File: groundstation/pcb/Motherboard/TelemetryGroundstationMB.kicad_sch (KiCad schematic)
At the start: 109 parts, among them J1 USB-C, J2 USB-C, J3 ICD15S13E4GV00LF, M1 M4 Mounting Hole, M2 M4 Mounting Hole, M3 M4 Mounting Hole, M4 M4 Mounting Hole, Q1 NPN, U1 CP2102N, U2 CP2102N, U5 AVR128DB64x-xPT

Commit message: update motherboard
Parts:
- removed D19, D20, D21, D22, D23, D24: red, LED_SMD:LED_0805_2012Metric_Pad1.15x1.40mm_HandSolder, symbol Device:LED
- removed D25, D26: orange, LED_SMD:LED_0805_2012Metric_Pad1.15x1.40mm_HandSolder, symbol Device:LED
- removed R32, R33, R35, R36, R43, R44: 1k, Resistor_SMD:R_0805_2012Metric_Pad1.20x1.40mm_HandSolder, symbol Device:R
- removed R34, R37, R38, R39, R40, R41, R42, R49, R50: 5k6, Resistor_SMD:R_0805_2012Metric_Pad1.20x1.40mm_HandSolder, symbol Device:R
- removed R45, R46: 270R, Resistor_SMD:R_0805_2012Metric_Pad1.20x1.40mm_HandSolder, symbol Device:R
- removed TP12, TP13, TP14, TP15, TP16, TP17, TP36, TP37, TP38, TP39, TP4, TP5, TP60, TP70, TP8, TP80, TP9: TestPoint, Footprints:Test Point, symbol Connector:TestPoint
- added C13, C14: 100uF Elko, Capacitor_THT:CP_Radial_D6.3mm_P2.50mm, symbol Device:C_Polarized
- added C5: 0.1 uF, Capacitor_SMD:C_0805_2012Metric_Pad1.18x1.45mm_HandSolder, symbol Device:C
- added C6: 4.7 uF, Capacitor_SMD:C_0805_2012Metric_Pad1.18x1.45mm_HandSolder, symbol Device:C
- added C7, C8: 10uF Tantal, Bibliothek:CAPMP3216X180N, symbol Device:C_Polarized
- added D14: SP0503BAHT, Package_TO_SOT_SMD:SOT-143, symbol Power_Protection:SP0503BAHT
- added D15: green, LED_SMD:LED_0805_2012Metric_Pad1.15x1.40mm_HandSolder, symbol Device:LED
- added D16, D29, D30, D31, D32, D33, D34: orange, LED_SMD:LED_0805_2012Metric_Pad1.15x1.40mm_HandSolder, symbol Device:LED
- added J4: USB-C, Footprints:GCT_USB4216-03-A_REVA, symbol Symbols:USB4216-03-A_REVA
- added J5, J6, J7: ICD15S13E4GV00LF, Footprints:AMPHENOL_ICD15S13E4GV00LF[1], symbol Symbols:ICD15S13E4GV00LF
- added J8: Conn_01x06_Pin, symbol Connector:Conn_01x06_Pin
- added JP3: SolderJumper_2_Open, Footprints:Solder Jumper, symbol Jumper:SolderJumper_2_Open
- added R22, R27: 5k1, Resistor_SMD:R_0805_2012Metric_Pad1.20x1.40mm_HandSolder, symbol Device:R
- added R23: 22k, Resistor_SMD:R_0805_2012Metric_Pad1.20x1.40mm_HandSolder, symbol Device:R
- added R24: 47k, Resistor_SMD:R_0805_2012Metric_Pad1.20x1.40mm_HandSolder, symbol Device:R
- added R25, R26: 560 Ohm, Resistor_SMD:R_0805_2012Metric_Pad1.20x1.40mm_HandSolder, symbol Device:R
- added R51, R52, R53, R54, R55, R56: 270R, Resistor_SMD:R_0805_2012Metric_Pad1.20x1.40mm_HandSolder, symbol Device:R
- added TP6, TP7: TestPoint, Footprints:Test Point, symbol Connector:TestPoint
- added U3: CP2102N, Footprints:QFN20_CP2102N_SIL, symbol Interface_USB:CP2102N-Axx-xQFN20
- added U4: MIC29300-5WU-TR, Footprints:MIC29300, symbol Symbols:MIC29300-3.3WU-TR
- added U6: MIC29300-3.3WU-TR, Footprints:MIC29300, symbol Symbols:MIC29300-3.3WU-TR
- D11, D12, R20, R21: now fitted
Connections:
- net D1 is gone; now on net D01: J3.1
- net D27 is gone; now on net D21: U5.49 (PF5)
- net MISO0 is gone; now on net RX4: U5.37 (PE1)
- net MOSI0 is gone; now on net TX4: U5.36 (PE0)
- net RST1 is gone; now on net D02: U5.1 (PA3)
- net RST2 is gone; now on net D31: U5.12 (PB4)
- net RTS2 is gone; now on net D31: U5.13 (PB5)
- net RX is gone; now on net RX0: J3.7
- net TX is gone; now on net TX0: J3.6
- net +3V3: now also C5.1, C6.1, C7.1, C8.1, D15.2 (A), D16.2 (A), J5.11, J5.5, J5.8, J6.11, J6.5, J6.8, J7.11, J7.5, J7.8, U3.6 (VDD), U3.7 (VREGIN), U4.3 (OUT), U6.3 (OUT)
- net +5V: now also J5.10, J5.13, J5.15, J6.10, J6.13, J6.15, J7.10, J7.13, J7.15
- net BUZZ: no longer U5.9 (PB1)
- net GND: now also C13.2, C14.2, C5.2, C6.2, C7.2, C8.2, D14.1 (A), D29.1 (K), D30.1 (K), D31.1 (K), D33.1 (K), D34.1 (K), J4.A1_B12 (GND_A), J4.B1_A12 (GND_B), J4.SH1 (SHIELD), J4.SH2 (SHIELD), J4.SH3 (SHIELD), J4.SH4 (SHIELD), J5.12, J5.14, J5.9, J5.SH1 (SHIELD), J5.SH2 (SHIELD__1), J6.12, J6.14, J6.9, J6.SH1 (SHIELD), J6.SH2 (SHIELD__1), J7.12, J7.14, J7.9, J7.SH1 (SHIELD), J7.SH2 (SHIELD__1), JP3.2 (B), R22.2, R24.2, R27.2, U3.12 (GND), U3.21 (GND), U3.3 (GND), U4.1 (IN), U4.4, U6.1 (IN), U6.4
- net LED 1: no longer U5.45 (XTAL32K2/PF1)
- net LED 2: no longer U5.46 (PF2)
- net LED 3: no longer U5.47 (PF3)
- net LED B: no longer U5.42 (PE6)
- net LED G: no longer U5.43 (PE7)
- net LED R: no longer U5.44 (XTAL32K1/PF0)
- net RX0: now also U5.63 (XTALHF2/PA1); no longer U5.3 (PA5)
- net RX1: now also J5.7
- net RX4: no longer U5.41 (PE5)
- net TX0: now also U5.62 (XTALHF1/PA0); no longer U5.2 (PA4)
- net TX1: now also J5.6
- net TX4: no longer U5.40 (PE4)
- net D31: now reaches U5.10 (PB2)
- net D31: now also U5.11 (PB3), J7.1
- net SDA0: now reaches U5.24 (PC6)
- net SDA0: now also R31.1
- net SCL0: now reaches U5.25 (PC7)
- net SCL0: now also R30.1
- net at U5.27 (PD1): now also R48.2
- net at U5.28 (PD2): now also R51.2
- net at U5.29 (PD3): now also R52.2
- net at U5.30 (PD4): now also R53.2
- net at U5.31 (PD5): now also R54.2
- net at U5.32 (PD6): now also R55.2; no longer R48.2
- net at U5.33 (VREFA/PD7): now also R56.2
- net at U5.54 (PG2): now also J8.1 (Pin_1)
- net at U5.55 (PG3): now also J8.2 (Pin_2)
- net at U5.58 (PG4): now also J8.3 (Pin_3)
- net at U5.59 (PG5): now also J8.4 (Pin_4)
- net at U5.60 (PG6): now also J8.5 (Pin_5)
- net at U5.61 (PG7): now also J8.6 (Pin_6)
- net D01: now reaches U5.64 (PA2)
- net ARM1 renamed RX5
- net RX5: now also TP7.1, U3.18 (TXD)
- net CFG1: no longer names the net of U5.5 (PA7)
- net CFG2: no longer names the net of U5.15 (PB7)
- net CS0 renamed LED2
- net CTS1: no longer names the net of U5.4 (PA6)
- net CTS2: no longer names the net of U5.14 (PB6)
- net D2 renamed D02
- net D26 renamed D21
- net D21: now also U5.46 (PF2), U5.47 (PF3), J6.1
- net D28: no longer names the net of U5.50 (~{RESET}/PF6)
- net D3 renamed D03
- net D03: now also U5.2 (PA4)
- net D4 renamed D04
- net D04: now also U5.3 (PA5); no longer U5.22 (PC4)
- net D5 renamed D14
- net D14: now also J5.4
- net RTS1 renamed TX3
- net TX3: now also J7.6
- net SCK0 renamed LED1
- net SCL1 renamed D12
- net D12: now also J5.2; no longer R30.1
- net SDA1 renamed D11
- net D11: now also J5.1; no longer R31.1
- net SLP renamed TX5
- net TX5: now also TP6.1, U3.17 (RXD)
- new net: D29.2 (A), R51.1
- new net: D30.2 (A), R52.1
- new net: R23.2, R24.1, U3.8 (VBUS)
- new net: D34.2 (A), R56.1
- new net: D32.2 (A), R54.1
- new net: J4.A5 (CC1), R22.1
- new net: J4.B5 (CC2), R27.1
- new net: D16.1 (K), R26.1
- new net: R26.2, U3.19 (~{RXT}/GPIO.3)
- new net: D33.2 (A), R55.1
- new net: D15.1 (K), R25.1
- new net: D31.2 (A), R53.1
- new net: JP3.1 (A), U3.15 (~{CTS})
- new net: R25.2, U3.20 (~{TXT}/GPIO.2)
- new net +BATT: C13.1, C14.1, U4.2 (GND), U6.2 (GND)
- new net D+3: D14.4 (K), J4.A6 (DP1), J4.B6 (DP2), U3.4 (D+)
- new net D-3: D14.3 (K), J4.A7 (DN1), J4.B7 (DN2), U3.5 (D-)
- new net D13: J5.3, U5.22 (PC4)
- new net D22: J6.2
- new net D23: J6.3
- new net D24: J6.4
- new net D32: J7.2
- new net D33: J7.3
- new net D34: J7.4
- new net LED3: U5.40 (PE4)
- new net LEDB: U5.41 (PE5)
- new net LEDG: U5.42 (PE6)
- new net LEDR: U5.43 (PE7)
- new net RX2: J6.7, U5.45 (XTAL32K2/PF1)
- new net RX3: J7.7, U5.9 (PB1)
- new net TX2: J6.6, U5.44 (XTAL32K1/PF0)
- new net VBUS3: D14.2 (K), J4.A4_B9 (VBUS_A), J4.B4_A9 (VBUS_B), R23.1
- no-connect marks 36 -> 28
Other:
- note added: "ESD Protection"
- note added: "HD15 D-SUB Connector"
- note added: "Power supply"
- note removed: "Pinheader?"
- note removed: "Test Points"
- moved on the sheet: J3, R30, R31

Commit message: update motherboard
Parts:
- removed D18: D, Diode_SMD:D_SOD-123, symbol Device:D
- removed LS1: Buzzer CMT-0525-75-SMT-TR, Footprints:Buzzer XDCR_CMT-0525-75-SMT-TR, symbol Symbols:Buzzer CMT-0525-75-SMT-TR
- removed Q1: NPN, Package_TO_SOT_SMD:SOT-23, symbol Simulation_SPICE:NPN
- removed R29: 180 R, Resistor_SMD:R_0805_2012Metric_Pad1.20x1.40mm_HandSolder, symbol Device:R
- added J9: Conn_01x04_Socket, symbol Connector:Conn_01x04_Socket
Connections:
- net +5V: now also J9.3 (Pin_3)
- net GND: now also J9.4 (Pin_4)
- net SCL0: now also J9.1 (Pin_1)
- net SDA0: now also J9.2 (Pin_2)
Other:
- note removed: "Buzzer"

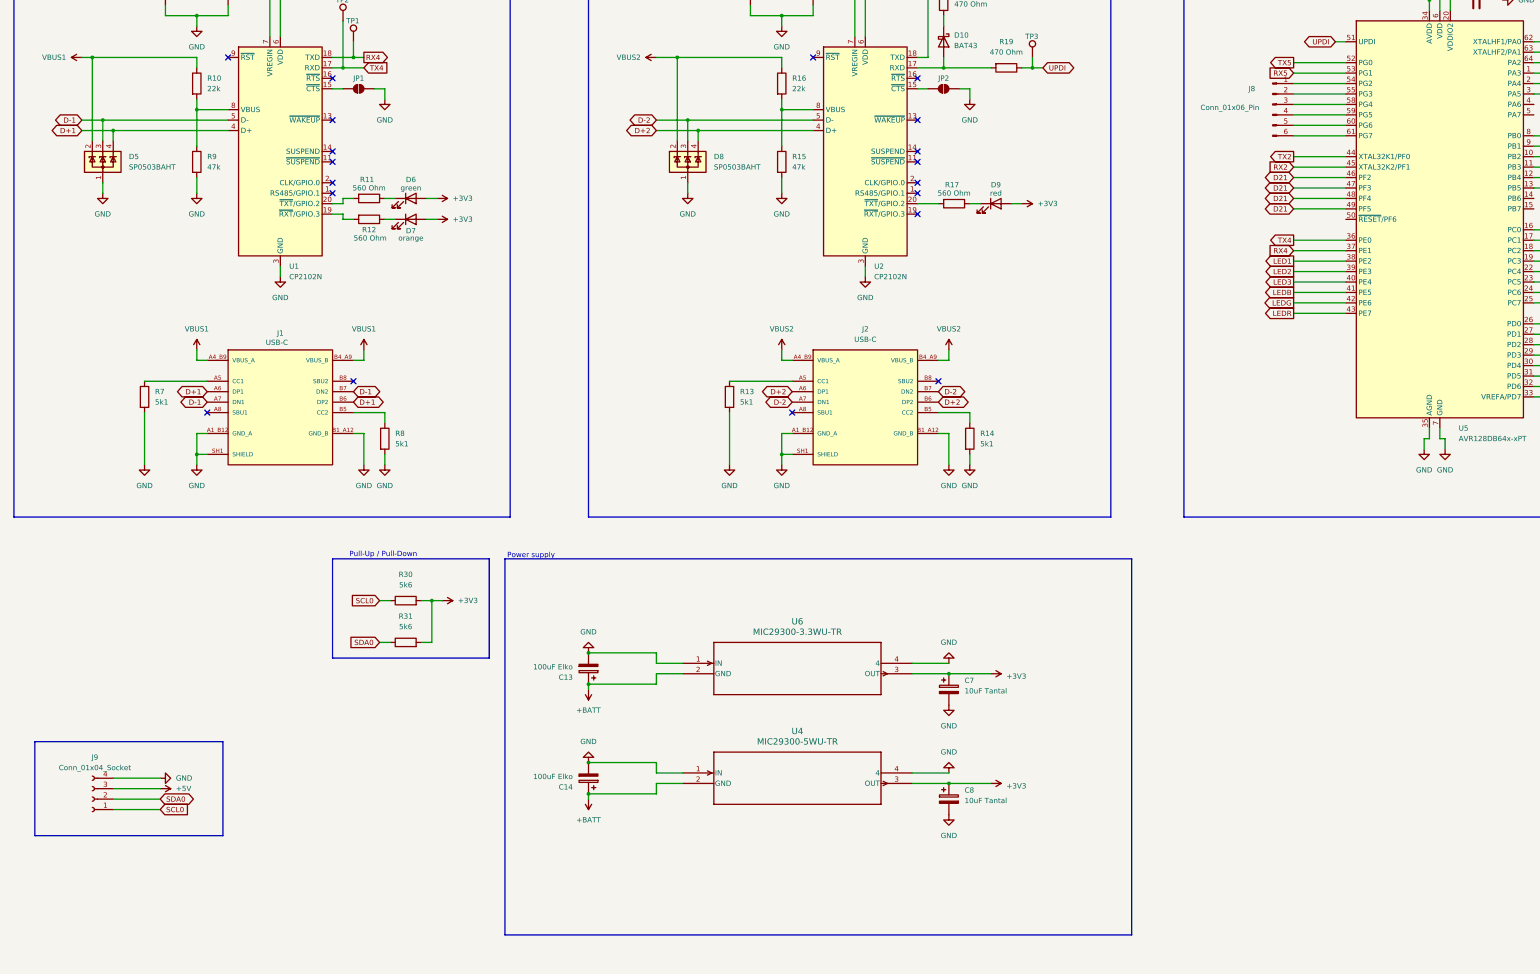
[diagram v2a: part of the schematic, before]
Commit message: add 6 buttons to motherboard
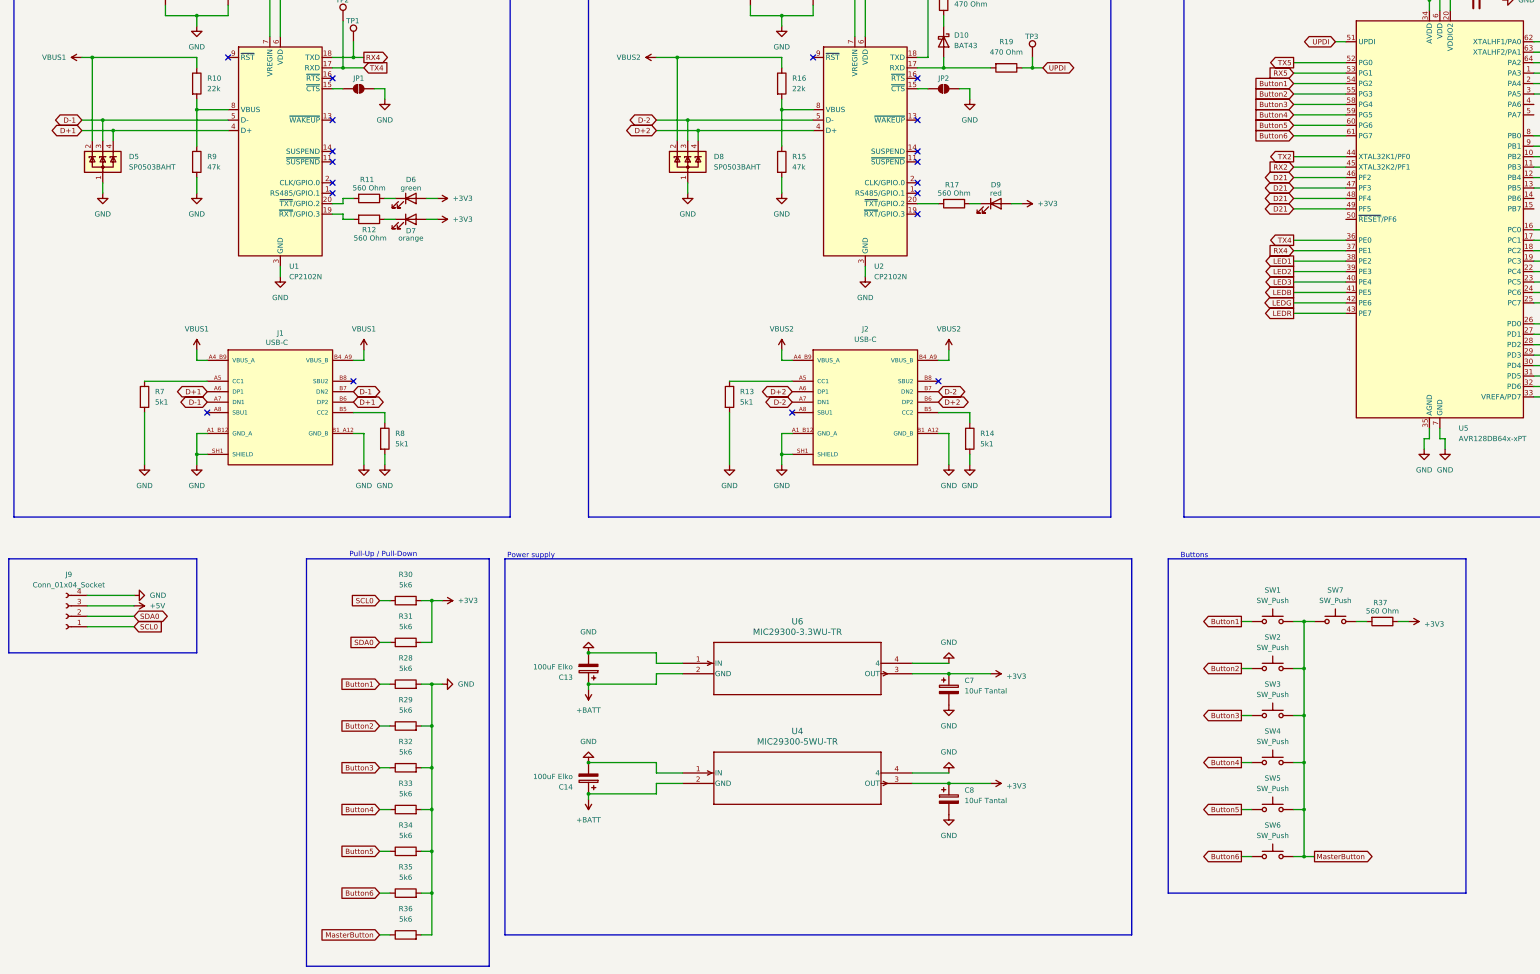
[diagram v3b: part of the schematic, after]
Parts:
- removed J8: Conn_01x06_Pin, symbol Connector:Conn_01x06_Pin
- added R28, R29, R32, R33, R34, R35, R36: 5k6, Resistor_SMD:R_0805_2012Metric_Pad1.20x1.40mm_HandSolder, symbol Device:R
- added R37: 560 Ohm, Resistor_SMD:R_0805_2012Metric_Pad1.20x1.40mm_HandSolder, symbol Device:R
- added SW1, SW2, SW3, SW4, SW5, SW6, SW7: SW_Push, symbol Switch:SW_Push
- R47, R48, R51, R52, R53, R54, R55, R56: value 270R -> 560 Ohm
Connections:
- net +3V3: now also R37.1
- net GND: now also R28.2, R29.2, R32.2, R33.2, R34.2, R35.2, R36.2
- net Button1: now reaches U5.54 (PG2)
- net Button1: now also R28.1, SW1.1
- net Button2: now reaches U5.55 (PG3)
- net Button2: now also R29.1, SW2.1
- net Button3: now reaches U5.58 (PG4)
- net Button3: now also R32.1, SW3.1
- net Button4: now reaches U5.59 (PG5)
- net Button4: now also R33.1, SW4.1
- net Button5: now reaches U5.60 (PG6)
- net Button5: now also R34.1, SW5.1
- net Button6: now reaches U5.61 (PG7)
- net Button6: now also R35.1, SW6.1
- new net: R37.2, SW7.2
- new net MasterButton: R36.1, SW1.2, SW2.2, SW3.2, SW4.2, SW5.2, SW6.2, SW7.1
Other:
- note added: "Buttons"
- moved on the sheet: J9

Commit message: include input from ignition system
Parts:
- added J8: Conn_01x03, symbol Connector_Generic:Conn_01x03
- added R38, R39: 5k6, Resistor_SMD:R_0805_2012Metric_Pad1.20x1.40mm_HandSolder, symbol Device:R
- added SW8: SW_DIP_x01, symbol Switch:SW_DIP_x01
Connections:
- net GND: now also J8.3 (Pin_3), R38.2, R39.2
- net Input1: now reaches U5.4 (PA6)
- net Input1: now also J8.1 (Pin_1), R38.1
- net Input2: now reaches U5.5 (PA7)
- net Input2: now also J8.2 (Pin_2), R39.1
- net at SW7.2: now also SW8.1; no longer R37.2
- new net: R37.2, SW8.2
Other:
- note added: "Display"
- note added: "From Ignition System"
- moved on the sheet: J9, R28, R29, R30, R31, R32, R33, R34, R35, R36, R37

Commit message: change hd15 pin positions
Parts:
- added J10, J11: Conn_01x01, symbol Connector_Generic:Conn_01x01
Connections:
- net +3V3: now also J3.10, J3.9, J5.10, J5.9, J6.10, J6.9, J7.10, J7.9; no longer J3.11, J3.5, J3.8, J5.11, J5.5, J5.8, J6.11, J6.5, J6.8, J7.11, J7.5, J7.8
- net +5V: now also J3.14, J5.14, J6.14, J7.14; no longer J3.10, J3.13, J5.10, J5.13, J6.10, J6.13, J7.10, J7.13
- net +BATT: now also J11.1 (Pin_1)
- net D01: now also J3.3; no longer J3.1
- net D02: now also J3.4; no longer J3.2
- net D03: now also J3.5; no longer J3.3
- net D04: now also J3.6; no longer J3.4
- net D11: now also J5.3; no longer J5.1
- net D12: now also J5.4; no longer J5.2
- net D13: now also J5.5; no longer J5.3
- net D14: now also J5.6; no longer J5.4
- net D21: now also J6.3; no longer J6.1
- net D22: now also J6.4; no longer J6.2
- net D23: now also J6.5; no longer J6.3
- net D24: now also J6.6; no longer J6.4
- net D31: now also J7.3; no longer J7.1
- net D32: now also J7.4; no longer J7.2
- net D33: now also J7.5; no longer J7.3
- net D34: now also J7.6; no longer J7.4
- net GND: now also J3.11, J3.13, J3.7, J3.8, J5.11, J5.13, J5.7, J5.8, J6.11, J6.13, J6.7, J6.8, J7.11, J7.13, J7.7, J7.8, J10.1 (Pin_1); no longer J3.14, J3.9, J5.14, J5.9, J6.14, J6.9, J7.14, J7.9
- net RX0: now also J3.2; no longer J3.7
- net RX1: now also J5.2; no longer J5.7
- net RX2: now also J6.2; no longer J6.7
- net RX3: now also J7.2; no longer J7.7
- net TX0: now also J3.1; no longer J3.6
- net TX1: now also J5.1; no longer J5.6
- net TX2: now also J6.1; no longer J6.6
- net TX3: now also J7.1; no longer J7.6
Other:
- note added: "Power Supply Connection"
- note added: "To Ignition System"

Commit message: add motherboard pcb
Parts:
- removed J8: Conn_01x03, symbol Connector_Generic:Conn_01x03
- added J8: LD09S33E4GV00LF, Footprints:AMPHENOL_LD09S33E4GV00LF, symbol Symbols:LD09S33E4GV00LF
- C7, C8: footprint Bibliothek:CAPMP3216X180N -> Footprints:CAPMP3216X180N
- J10, J11: footprint (none) -> Footprints:Banana_CT3151-0
- J9: footprint (none) -> Connector_PinSocket_2.54mm:PinSocket_1x04_P2.54mm_Vertical
- SW1, SW2, SW3, SW4, SW5, SW6, SW7, SW8: footprint (none) -> Connector_PinSocket_2.54mm:PinSocket_1x02_P2.54mm_Vertical
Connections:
- net LED1 is gone; now on net D23: U5.38 (PE2)
- net LED2 is gone; now on net D22: U5.39 (PE3)
- net LED3 is gone; now on net D21: U5.40 (PE4)
- net LEDB is gone; now on net D24: U5.41 (PE5)
- net LEDG is gone; now on net Input2: U5.42 (PE6)
- net LEDR is gone; now on net Input1: U5.43 (PE7)
- net +3V3: no longer C8.1, U4.3 (OUT)
- net +5V: now also C8.1, U4.3 (OUT)
- net Button2: now also U5.50 (~{RESET}/PF6); no longer U5.55 (PG3)
- net Button3: now also U5.49 (PF5); no longer U5.58 (PG4)
- net Button4: now also U5.48 (PF4); no longer U5.59 (PG5)
- net Button5: now also U5.47 (PF3); no longer U5.60 (PG6)
- net Button6: now also U5.46 (PF2); no longer U5.61 (PG7)
- net D01: now also U5.1 (PA3); no longer U5.64 (PA2)
- net D02: now also U5.64 (PA2); no longer U5.1 (PA3)
- net D03: now also U5.63 (XTALHF2/PA1); no longer U5.2 (PA4)
- net D04: now also U5.4 (PA6); no longer U5.3 (PA5)
- net D11: now also U5.22 (PC4); no longer U5.18 (PC2)
- net D13: now also U5.18 (PC2); no longer U5.22 (PC4)
- net D21: no longer U5.46 (PF2), U5.47 (PF3), U5.48 (PF4), U5.49 (PF5)
- net D31: no longer U5.10 (PB2), U5.11 (PB3), U5.13 (PB5)
- net D32: now also U5.11 (PB3)
- net D33: now also U5.10 (PB2)
- net D34: now also U5.13 (PB5)
- net GND: now also D32.1 (K), J8.5, J8.SH1 (SHIELD), J8.SH2 (SHIELD__1)
- net Input1: now also J8.3; no longer U5.4 (PA6)
- net Input2: now also J8.4; no longer U5.5 (PA7)
- net LED 1: now also U5.62 (XTALHF1/PA0)
- net LED 2: now also U5.61 (PG7)
- net LED 3: now also U5.60 (PG6)
- net LED B: now also U5.55 (PG3)
- net LED G: now also U5.58 (PG4)
- net LED R: now also U5.59 (PG5)
- net RX0: now also U5.3 (PA5); no longer U5.63 (XTALHF2/PA1)
- net RX2: now also TP7.1, U3.18 (TXD); no longer J6.2
- net RX4: now also J6.2; no longer TP1.1, U1.18 (TXD)
- net RX5: now also TP1.1, U1.18 (TXD); no longer TP7.1, U3.18 (TXD)
- net TX0: now also U5.2 (PA4); no longer U5.62 (XTALHF1/PA0)
- net TX2: now also TP6.1, U3.17 (RXD); no longer J6.1
- net TX4: now also J6.1; no longer TP2.1, U1.17 (RXD)
- net TX5: now also TP2.1, U1.17 (RXD); no longer TP6.1, U3.17 (RXD)
- no-connect marks 28 -> 37

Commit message: add power supply via USB to Motherboard
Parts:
- removed C14: 100uF Elko, Capacitor_THT:CP_Radial_D6.3mm_P2.50mm, symbol Device:C_Polarized
- removed C8: 10uF Tantal, Footprints:CAPMP3216X180N, symbol Device:C_Polarized
- removed U4: MIC29300-5WU-TR, Footprints:MIC29300, symbol Symbols:MIC29300-3.3WU-TR
- added J12: USB-C, Footprints:GCT_USB4216-03-A_REVA, symbol Symbols:USB4216-03-A_REVA
- added R40, R41: 5k1, Resistor_SMD:R_0805_2012Metric_Pad1.20x1.40mm_HandSolder, symbol Device:R
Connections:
- net +5V: now also C13.1, J11.1 (Pin_1), U6.2 (GND), J12.A4_B9 (VBUS_A), J12.B4_A9 (VBUS_B)
- net +BATT: no longer C13.1, J11.1 (Pin_1), U6.2 (GND)
- net GND: now also J12.A1_B12 (GND_A), J12.B1_A12 (GND_B), J12.SH1 (SHIELD), J12.SH2 (SHIELD), J12.SH3 (SHIELD), J12.SH4 (SHIELD), R40.2, R41.2
- new net: J12.A5 (CC1), R40.1
- new net: J12.B5 (CC2), R41.1
- no-connect marks 37 -> 43
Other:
- moved on the sheet: C13, C7, U6

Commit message: finishing touches to motherboard
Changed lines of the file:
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@@
 	)
 	(symbol
-		(lib_id "power:+BATT")
-		(at 495.3 111.76 270)
-		(unit 1)
-		(exclude_from_sim no)
-		(in_bom yes)
-		(on_board yes)
-		(dnp no)
-		(fields_autoplaced yes)
-		(property "Reference" "#PWR0148"
-			(at 491.49 111.76 0)
-			(effects
-				(font
-					(size 1.27 1.27)
-				)
-				(hide yes)
-			)
-		)
-		(property "Value" "+BATT"
-			(at 499.11 111.7599 90)
-			(effects
-				(font
-					(size 1.27 1.27)
-				)
-				(justify left)
-			)
-		)
-		(property "Footprint" ""
-			(at 495.3 111.76 0)
-			(effects
-				(font
-					(size 1.27 1.27)
-				)
-				(hide yes)
-			)
-		)
-		(property "Datasheet" ""
-			(at 495.3 111.76 0)
-			(effects
-				(font
-					(size 1.27 1.27)
-				)
-				(hide yes)
-			)
-		)
-		(property "Description" "Power symbol creates a global label with name \"+BATT\""
-			(at 495.3 111.76 0)
-			(effects
-				(font
-					(size 1.27 1.27)
-				)
-				(hide yes)
-			)
-		)
-		(pin "1"
-		)
-		(instances
-			(project "TelemetryGroundstationMB"
-				(path "/a51e9d97-2dc7-47e6-bab2-df98d7ad5ab9"
-					(reference "#PWR0148")
-					(unit 1)
-				)
-			)
-		)
-	)
-	(symbol
 		(lib_id "power:GND")
 		(at 494.03 217.17 0)
@@
 					(unit 1)
 				)
-			)
-		)
-	)
-	(symbol
-		(lib_id "power:PWR_FLAG")
-		(at 495.3 111.76 90)
-		(unit 1)
-		(exclude_from_sim no)
-		(in_bom yes)
-		(on_board yes)
-		(dnp no)
-		(fields_autoplaced yes)
-		(property "Reference" "#FLG08"
-			(at 493.395 111.76 0)
-			(effects
-				(font
-					(size 1.27 1.27)
-				)
-				(hide yes)
-			)
-		)
-		(property "Value" "PWR_FLAG"
-			(at 491.49 111.7599 90)
-			(effects
-				(font
-					(size 1.27 1.27)
-				)
-				(justify left)
-			)
-		)
-		(property "Footprint" ""
-			(at 495.3 111.76 0)
-			(effects
-				(font
-					(size 1.27 1.27)
-				)
-				(hide yes)
-			)
-		)
-		(property "Datasheet" "~"
-			(at 495.3 111.76 0)
-			(effects
-				(font
-					(size 1.27 1.27)
-				)
-				(hide yes)
-			)
-		)
-		(property "Description" "Special symbol for telling ERC where power comes from"
-			(at 495.3 111.76 0)
-			(effects
-				(font
-					(size 1.27 1.27)
-				)
-				(hide yes)
-			)
-		)
-		(pin "1"
-		)
-		(instances
-			(project ""
-				(path "/a51e9d97-2dc7-47e6-bab2-df98d7ad5ab9"
-					(reference "#FLG08")
-					(unit 1)
-				)
